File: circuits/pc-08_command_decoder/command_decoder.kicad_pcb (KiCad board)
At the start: 2 copper layers, 99.1 x 99.1 mm, 34 parts, among them J1 Screw_Terminal_01x02, J2 Conn_01x06, J3 Conn_01x03, J4 Conn_01x08, J5 Conn_01x05, J6 Conn_01x07, U1 74HC138, U2 74HC138, U3 74HC138, U4 74HC138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

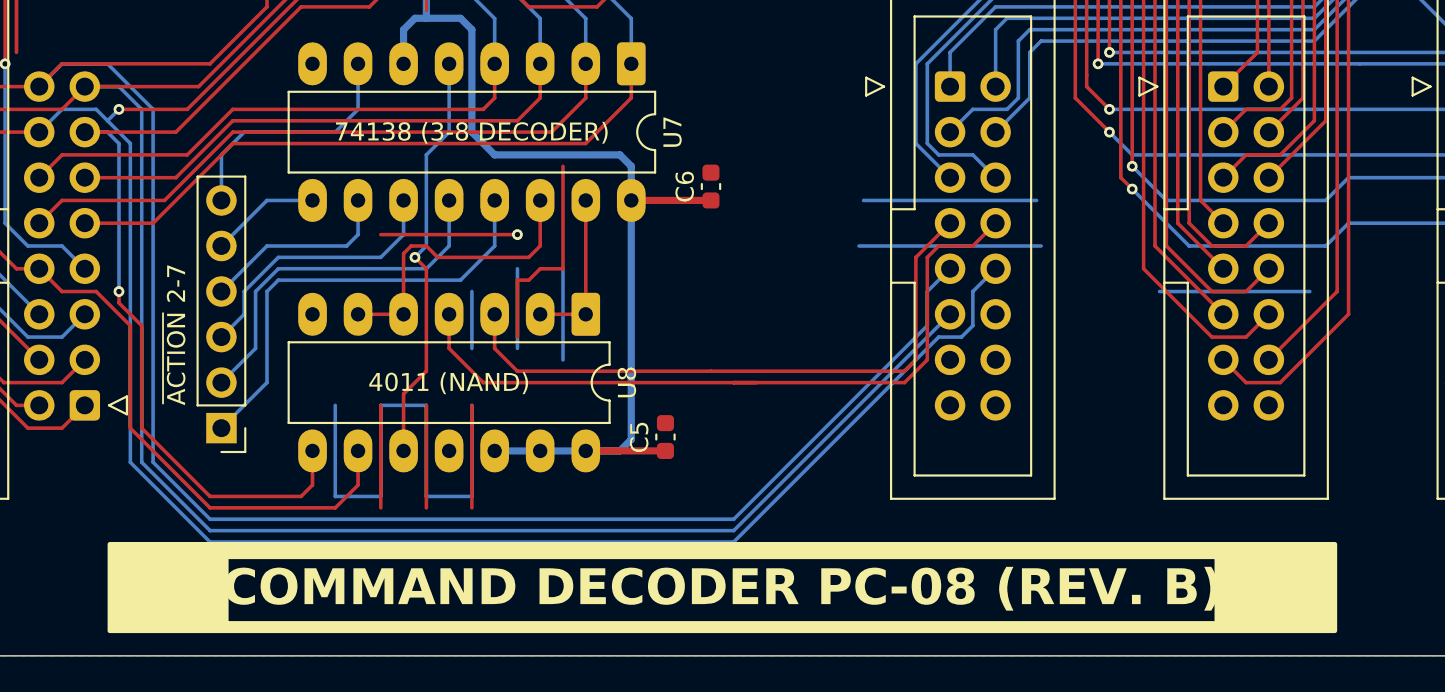
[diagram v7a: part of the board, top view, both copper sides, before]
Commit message: add IPC write to command decoder and 16-bit control bus.
This signal may be used in the future for interrupt handling.
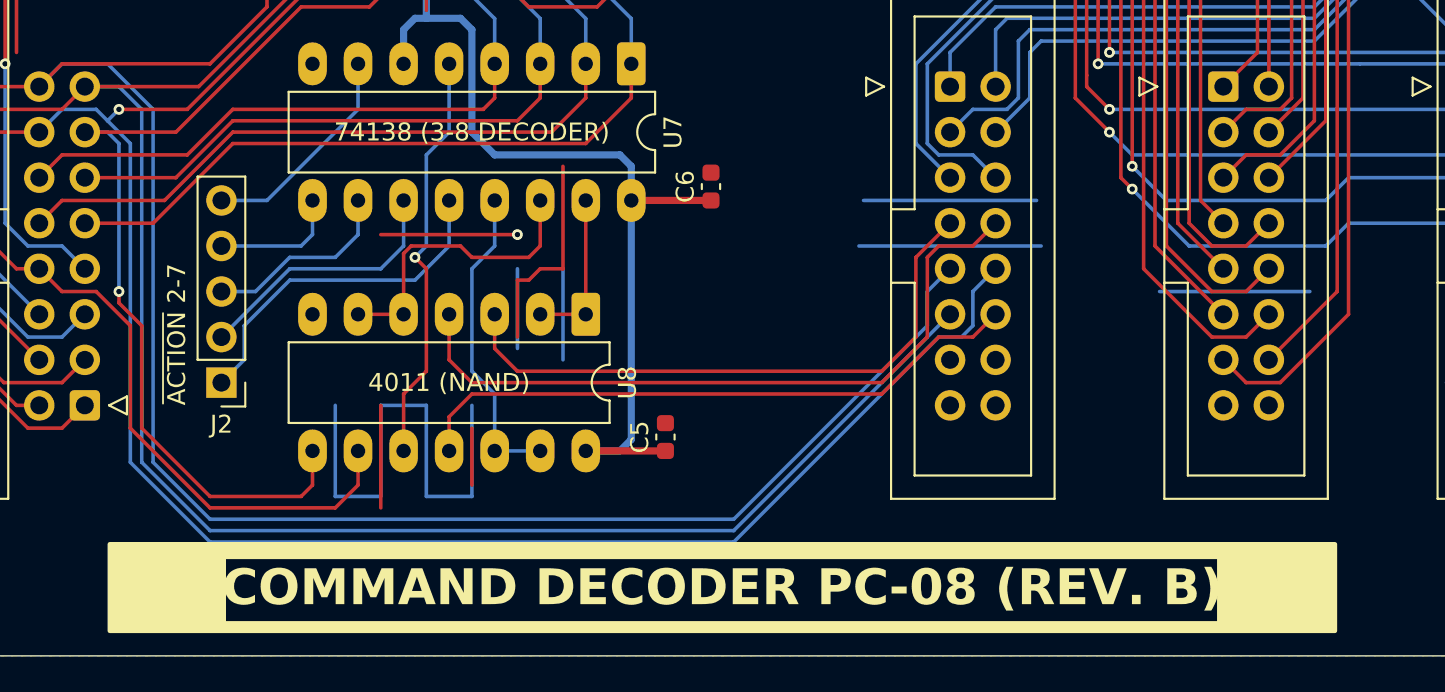
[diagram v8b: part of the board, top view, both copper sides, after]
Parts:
- J2: value Conn_01x06 -> Conn_01x05; footprint Connector_PinHeader_2.54mm:PinHeader_1x06_P2.54mm_Vertical -> Connector_PinHeader_2.54mm:PinHeader_1x05_P2.54mm_Vertical
- moved J2 2.54 mm to (62.2, 106.7)
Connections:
- CTRL_BUS2 pad 12: unconnected-(CTRL_BUS2-Pin_12-Pad12) -> /writeIPC
- J2 pad 1: Net-(J2-Pin_1) -> /~{action_channel_3}
- J2 pad 2: Net-(J2-Pin_2) -> /~{action_channel_4}
- J2 pad 3: Net-(J2-Pin_3) -> /~{action_channel_5}
- J2 pad 4: Net-(J2-Pin_4) -> /~{action_channel_6}
- J2 pad 5: Net-(J2-Pin_5) -> /~{action_channel_7}
- U7 pad 10: Net-(J2-Pin_4) -> /~{action_channel_5}
- U7 pad 11: Net-(J2-Pin_3) -> /~{action_channel_4}
- U7 pad 12: Net-(J2-Pin_2) -> /~{action_channel_3}
- U7 pad 13: Net-(J2-Pin_1) -> /~{writeIPC}
- U7 pad 7: Net-(J2-Pin_6) -> /~{action_channel_7}
- U7 pad 9: Net-(J2-Pin_5) -> /~{action_channel_6}
- U8 pad 11: unconnected-(U8-Pad11) -> /writeIPC
- U8 pad 12: VCC -> /~{writeIPC}
- U8 pad 13: VCC -> /~{writeIPC}
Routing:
- net /writeIPC: track 0.00 -> 34.8 mm
- net Net-(J2-Pin_1): track 25.0 -> 0.00 mm
- net Net-(J2-Pin_2): track 20.3 -> 0.00 mm
- net /~{action_channel_3}: track 0.00 -> 19.5 mm
- net /~{writeIPC}: track 0.00 -> 17.1 mm
- net Net-(J2-Pin_3): track 15.2 -> 0.00 mm
- net /~{action_channel_4}: track 0.00 -> 14.8 mm
- net Net-(J2-Pin_6): track 13.8 -> 0.00 mm
- net /~{action_channel_7}: track 0.00 -> 12.3 mm
- net GND: track 347.3 -> 335.8 mm
- net Net-(J2-Pin_4): track 10.8 -> 0.00 mm
- net /~{action_channel_5}: track 0.00 -> 10.8 mm
- net /~{action_channel_6}: track 0.00 -> 7.25 mm
- net Net-(J2-Pin_5): track 6.13 -> 0.00 mm
- net VCC: track 310.8 -> 305.8 mm
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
